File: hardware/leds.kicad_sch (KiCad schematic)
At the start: 55 parts, among them J10 Conn_01x02, J11 Conn_01x02, J12 Conn_01x02, J13 Conn_01x02, J4 Conn_01x02, J5 Conn_01x02, J6 Conn_01x02, J7 Conn_01x02, J8 Conn_01x02, J9 Conn_01x02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

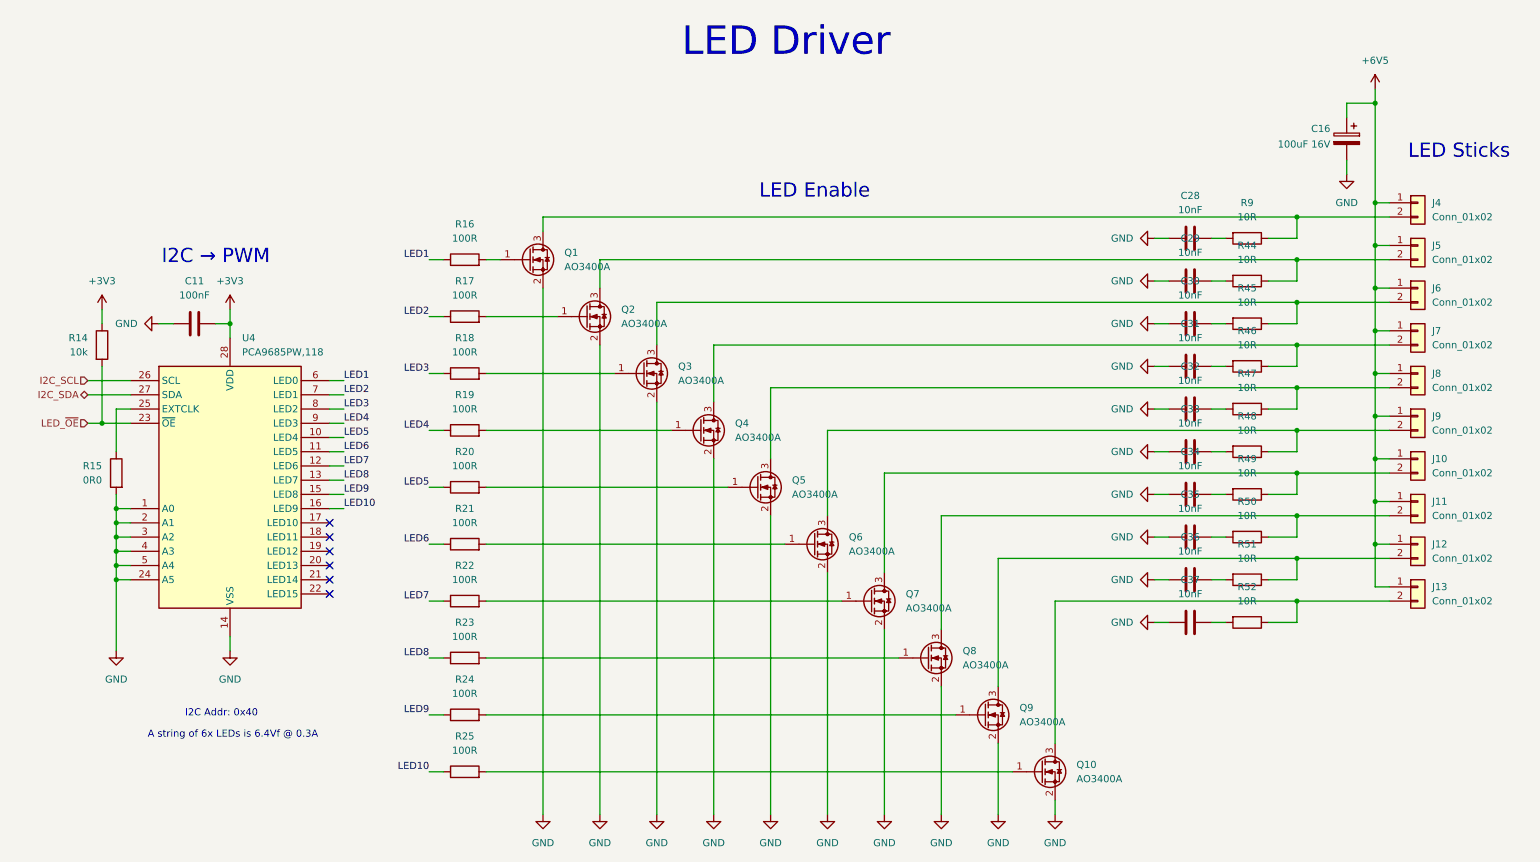
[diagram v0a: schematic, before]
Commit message: reviewed LED connections and found a fault
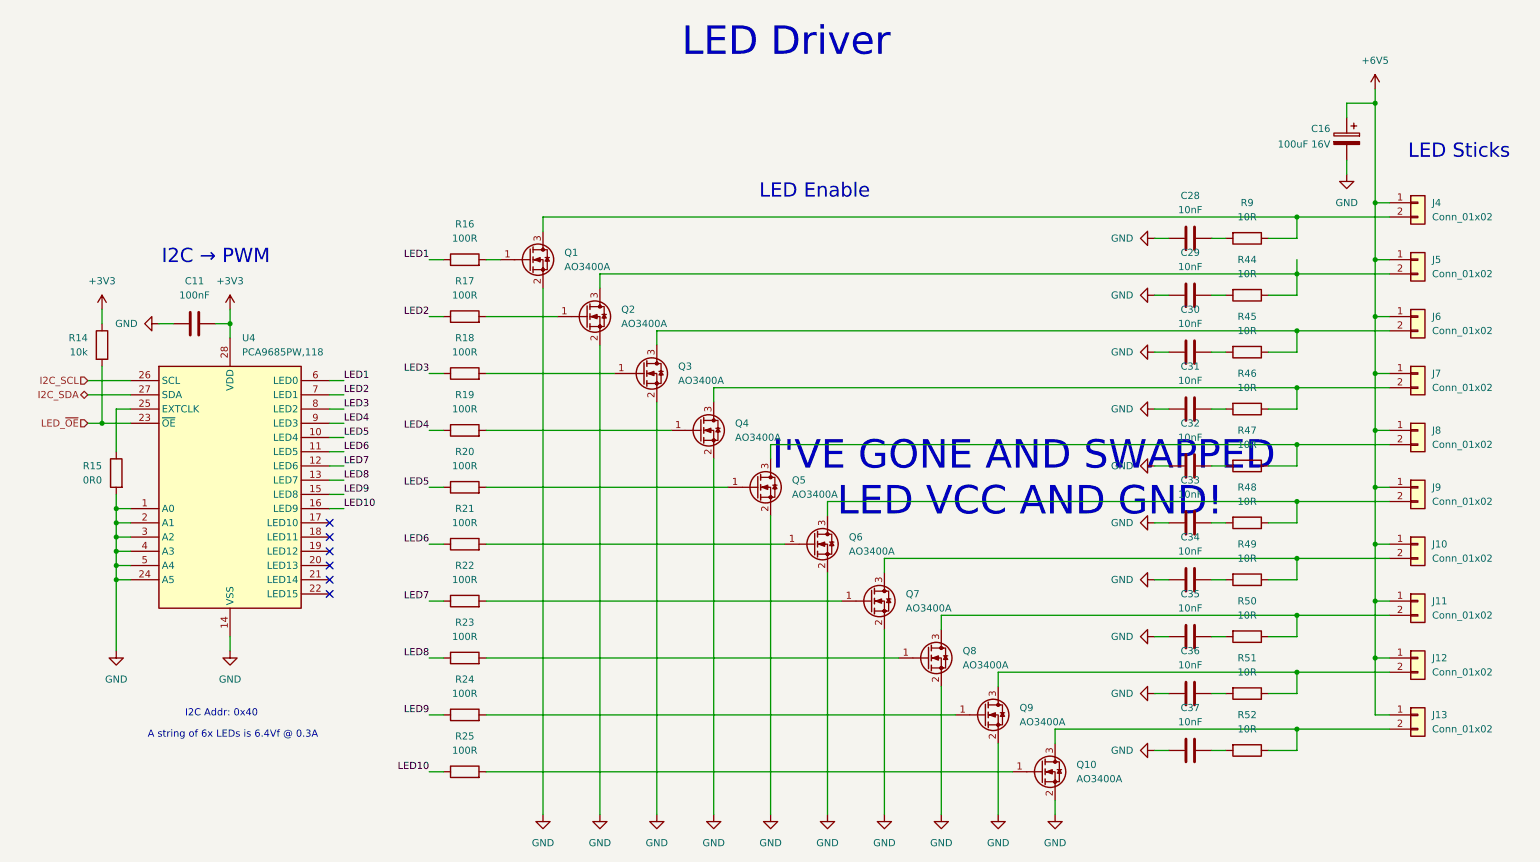
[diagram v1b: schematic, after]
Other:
- note added: "I'VE GONE AND SWAPPED LED VCC AND GND!"
- moved on the sheet: C29, C30, C31, C32, C33, C34, C35, C36, C37, J10, J11, J12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

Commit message: unswapped LEDs
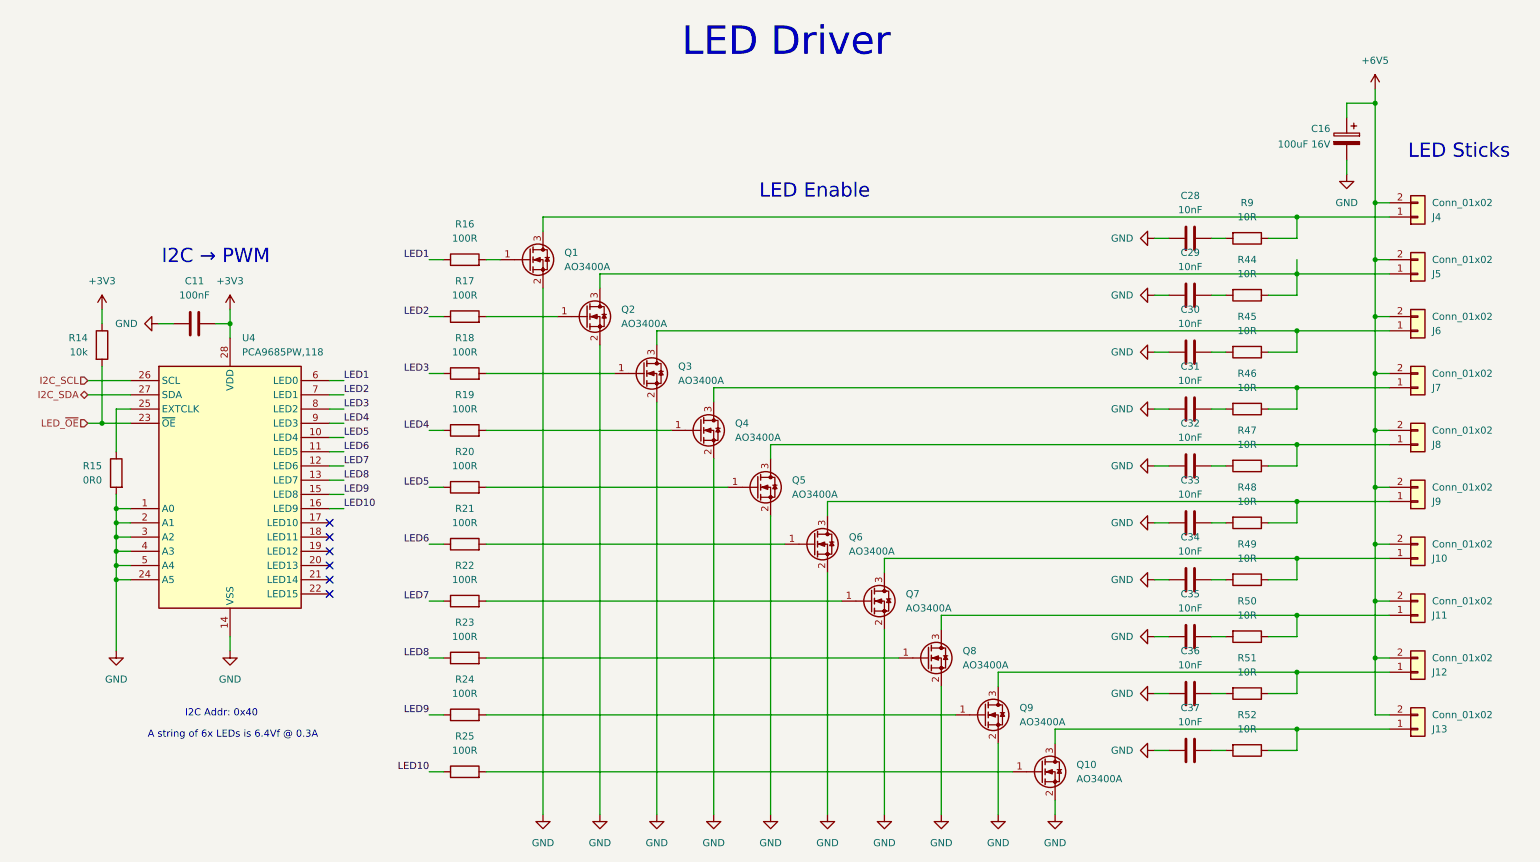
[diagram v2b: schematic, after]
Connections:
- net +6V5: now also J10.2 (Pin_2), J11.2 (Pin_2), J12.2 (Pin_2), J13.2 (Pin_2), J4.2 (Pin_2), J5.2 (Pin_2), J6.2 (Pin_2), J7.2 (Pin_2), J8.2 (Pin_2), J9.2 (Pin_2); no longer J10.1 (Pin_1), J11.1 (Pin_1), J12.1 (Pin_1), J13.1 (Pin_1), J4.1 (Pin_1), J5.1 (Pin_1), J6.1 (Pin_1), J7.1 (Pin_1), J8.1 (Pin_1), J9.1 (Pin_1)
- net at Q10.3 (D), R52.1: now also J13.1 (Pin_1); no longer J13.2 (Pin_2)
- net at Q9.3 (D), R51.1: now also J12.1 (Pin_1); no longer J12.2 (Pin_2)
- net at Q2.3 (D), R44.1: now also J5.1 (Pin_1); no longer J5.2 (Pin_2)
- net at Q7.3 (D), R49.1: now also J10.1 (Pin_1); no longer J10.2 (Pin_2)
- net at Q4.3 (D), R46.1: now also J7.1 (Pin_1); no longer J7.2 (Pin_2)
- net at Q6.3 (D), R48.1: now also J9.1 (Pin_1); no longer J9.2 (Pin_2)
- net at Q1.3 (D), R9.1: now also J4.1 (Pin_1); no longer J4.2 (Pin_2)
- net at Q5.3 (D), R47.1: now also J8.1 (Pin_1); no longer J8.2 (Pin_2)
- net at Q8.3 (D), R50.1: now also J11.1 (Pin_1); no longer J11.2 (Pin_2)
- net at Q3.3 (D), R45.1: now also J6.1 (Pin_1); no longer J6.2 (Pin_2)
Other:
- note removed: "I'VE GONE AND SWAPPED LED VCC AND GND!"

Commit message: preparing for release
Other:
- title: (none) -> LEDs
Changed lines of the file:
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@@
 	(paper "A4")
 	(title_block
-		(date "2026-04-10")
-		(rev "0")
+		(title "LEDs")
+		(date "2026-06-05")
+		(rev "1")
 		(company "Wires & Bits")
 	)
